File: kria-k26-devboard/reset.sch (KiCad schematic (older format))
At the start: 0 parts

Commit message: Finished reset logic, added crystal gen. to USB PHY, create power toggle for SD 3.0
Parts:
- added C? (x2): C_47n_0402, antmicro-footprints:0402-cap, symbol antmicroCapacitors0402:C_47n_0402
- added C? (x7): C_100n_0402, antmicro-footprints:0402-cap, symbol antmicroCapacitors0402:C_100n_0402
- added R? (x5): R_10k_0402, antmicro-footprints:0402-res, symbol antmicroResistors0402:R_10k_0402
- added S?: KMR2, antmicro-footprints:SW_SPST_4.2x2.8, symbol antmicroPushbuttonSwitches:KMR2
- added U? (x2): TPS3840PH30DBVR, antmicro-footprints:SOT-23-5, symbol antmicroPMICPowerSequencers:TPS3840PH30DBVR
- added U? (x2): SN74AVC4T245PWR, Package_SO:TSSOP-16_4.4x5mm_P0.65mm, symbol antmicroLogicTranslatorsLevelShifters:SN74AVC4T245PWR
- added U? (x6): 74LV07ATPWJ, antmicro-footprints:TSSOP-14_W4.4mm, symbol antmicroLogicGatesandInverters:74LV07ATPWJ
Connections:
- new net: S?.2, S?.4, U?.4 (MR_N), U?.4 (MR_N)
- new net: U?.1 (RESET), U?.14 (2~OE), U?.15 (1~OE) (x2)
- new net: C?.1, U?.5 (CT) (x2)
- new net: U?.1, U?.4 (1A1)
- new net: U?.3, U?.5 (1A2)
- new net: U?.5, U?.6 (2A1)
- new net: U?.7 (2A2), U?.9
- new net: U?.11, U?.4 (1A1)
- new net CAM0_PWDN: U?.5 (1A2)
- new net CAM0_RST: R?.2, U?.10
- new net CAM1_PWDN: U?.6 (2A1)
- new net ETH_RESET: R?.2, U?.8
- new net GND: C?.2, C?.2, C?.2, C?.2, C?.2, C?.2, C?.2, C?.2, C?.2, S?.1, S?.3, U?.10 (2B2), U?.2 (1DIR), U?.2 (1DIR), U?.3 (2DIR), U?.3 (2DIR), U?.3 (GND), U?.3 (GND), U?.7 (GND), U?.8 (GND), U?.8 (GND), U?.9 (GND), U?.9 (GND)
- new net HDA02: U?.13 (1B1)
- new net HDA04: U?.12 (1B2)
- new net HDA09: U?.11 (2B1)
- new net MIO38: U?.10 (2B2)
- new net MIO43: U?.13 (1B1)
- new net MIO44: U?.11 (2B1), U?.12 (1B2)
- new net PL_1V8: U?.16 (VCCB)
- new net PL_3V3: R?.1, U?.2 (VDD)
- new net PS_1V8: C?.1, C?.1, R?.1, R?.1, U?.16 (VCCB)
- new net PS_3V3: C?.1, C?.1, C?.1, C?.1, R?.1, R?.1, U?.1 (VCCA), U?.1 (VCCA), U?.2 (VDD)
- new net SD_CARD_RESET: R?.2, U?.2
- new net SOM_5V: C?.1, U?.14 (VCC)
- new net USB_HUB_RESET: R?.2, U?.6
- new net USB_PHY_RESET: R?.2, U?.4

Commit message: Progress on Debug sheet
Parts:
- gave numbers to parts that had none: 20

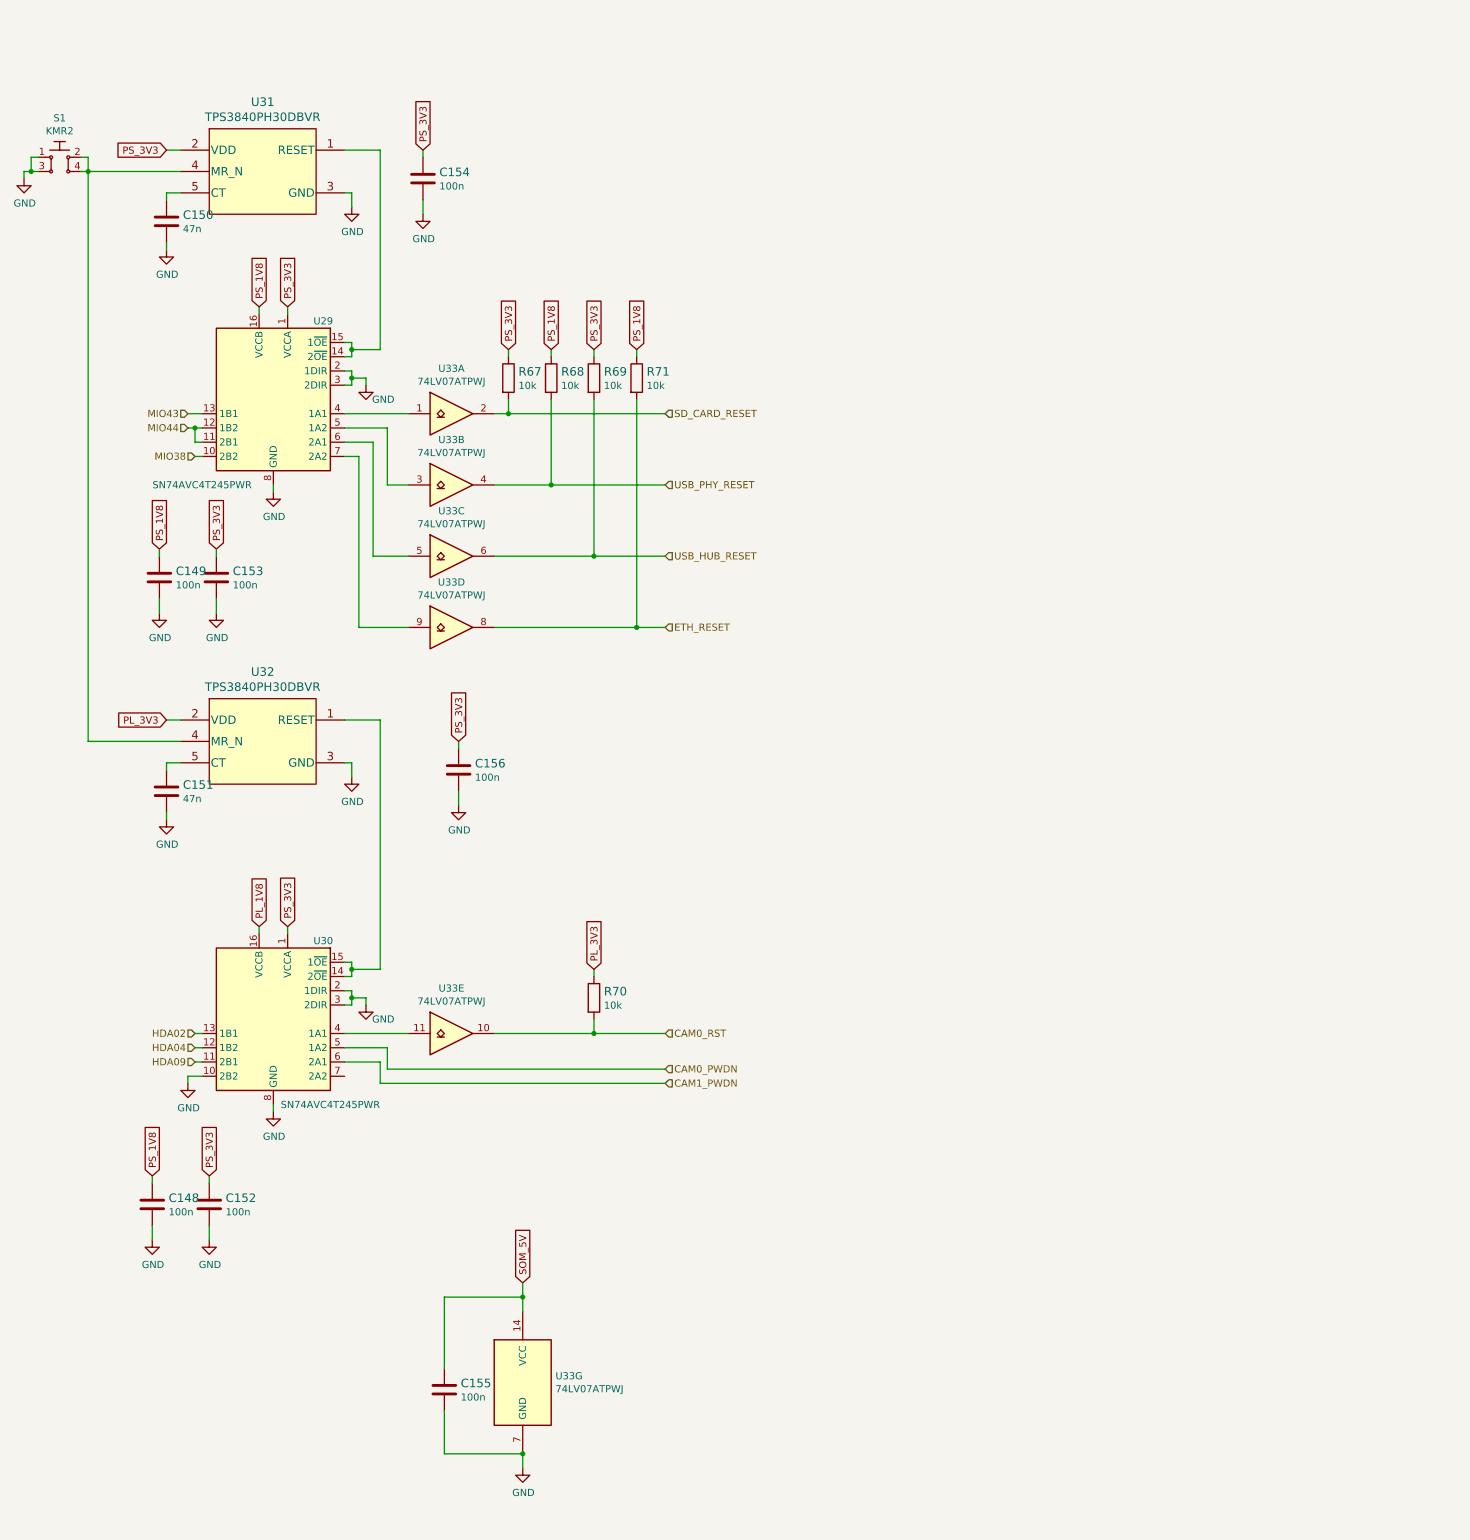
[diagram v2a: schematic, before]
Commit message: Added finished i2c (wirh eeprom) and pmod sheet. Added JTAG connector with collision avoidance logic
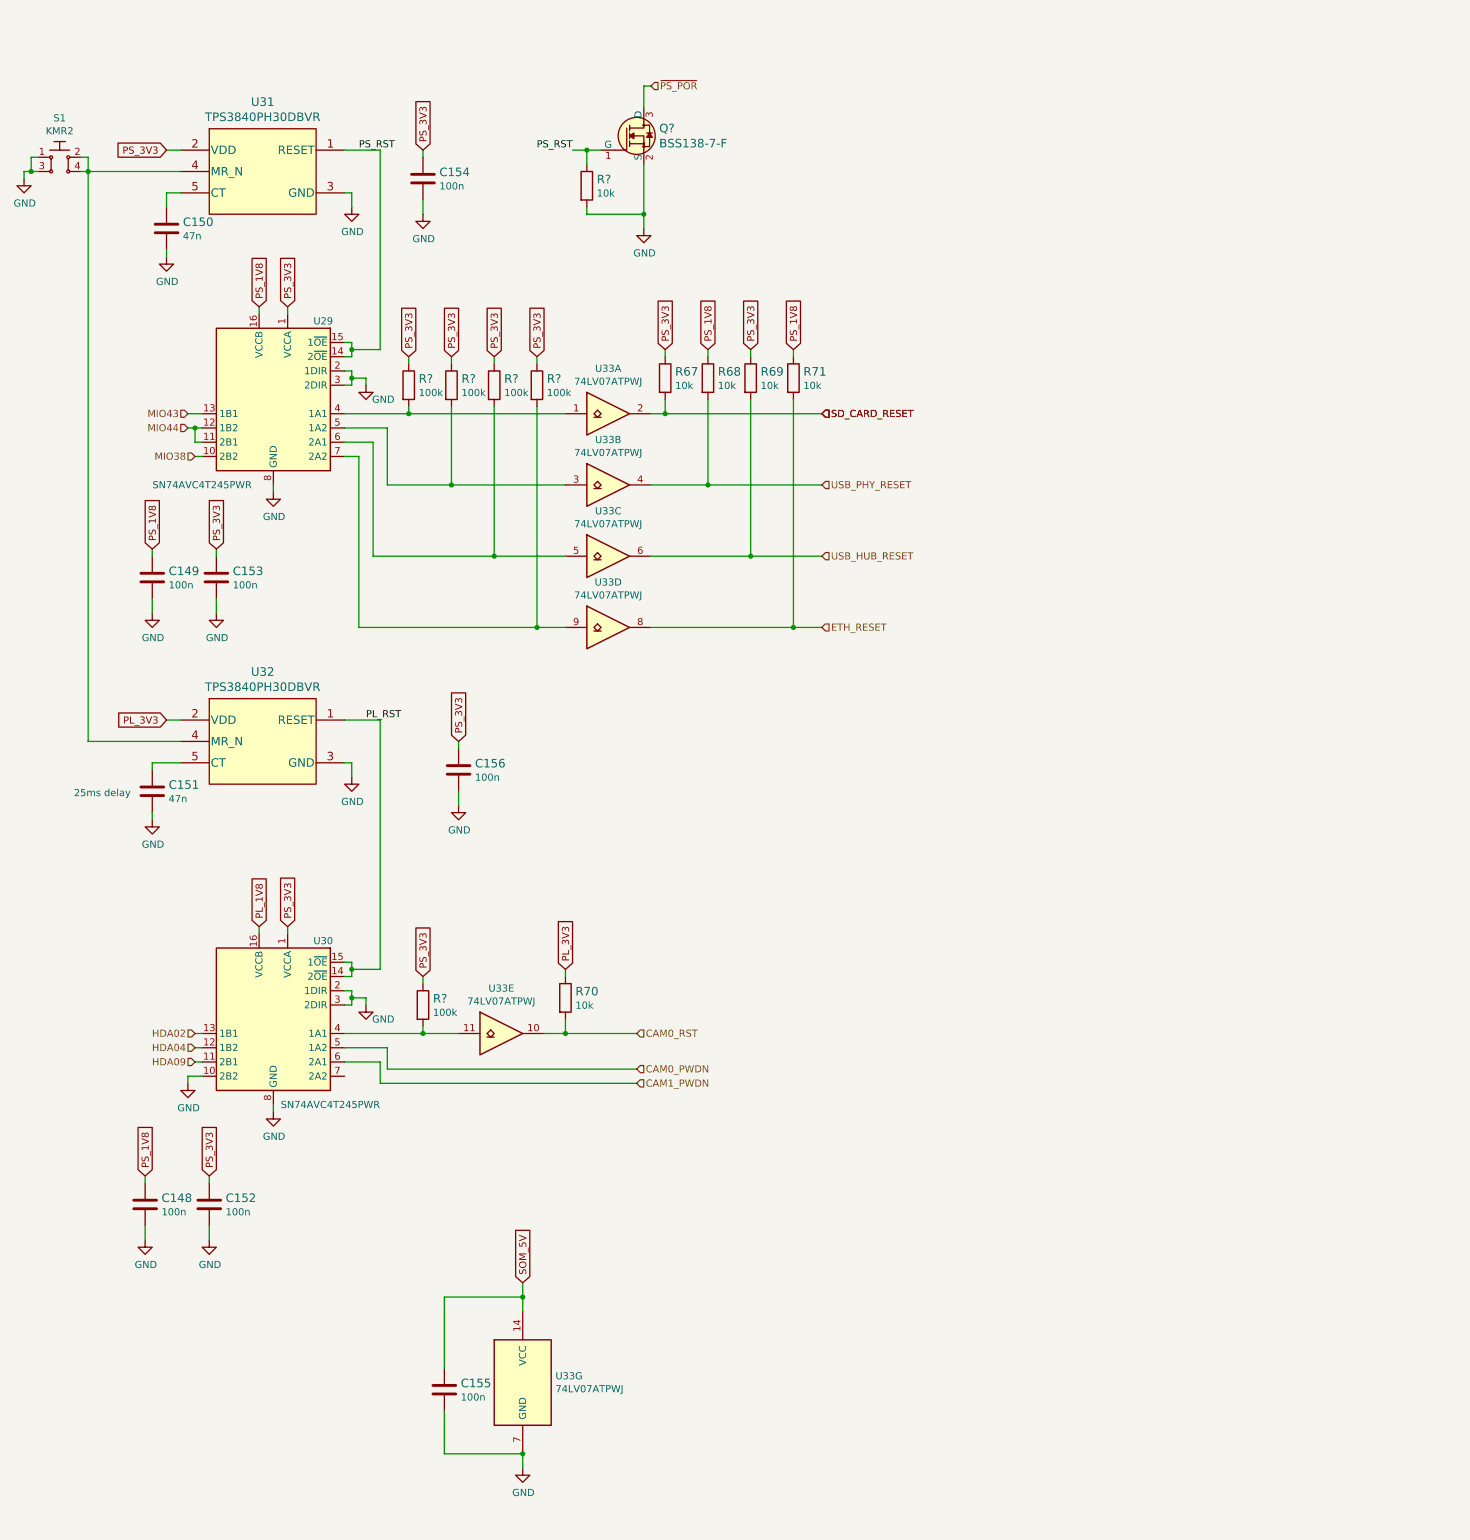
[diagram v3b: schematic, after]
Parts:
- added Q?: BSS138-7-F, antmicro-footprints:SOT-23-3, symbol antmicroTransistorsFETsMOSFETsSingle:BSS138-7-F
- added R?: R_10k_0402, antmicro-footprints:0402-res, symbol antmicroResistors0402:R_10k_0402
- added R? (x5): R_100k_0402, antmicro-footprints:0402-res, symbol antmicroResistors0402:R_100k_0402
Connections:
- net GND: now also Q?.2 (S), R?.2
- net PS_3V3: now also R?.1, R?.1, R?.1, R?.1, R?.1
- net PS_RST: now reaches U29.14 (2~OE), U29.15 (1~OE), U31.1 (RESET)
- net PS_RST: now also Q?.1 (G), R?.1
- net PL_RST: now reaches U30.14 (2~OE), U30.15 (1~OE), U32.1 (RESET)
- net at U29.4 (1A1), U33.1: now also R?.2
- net at U29.5 (1A2), U33.3: now also R?.2
- net at U29.6 (2A1), U33.5: now also R?.2
- net at U29.7 (2A2), U33.9: now also R?.2
- net at U30.4 (1A1), U33.11: now also R?.2
- new net ~PS_POR: Q?.3 (D)
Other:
- note added: "25ms delay"
- moved on the sheet: C148, C149, C150, C151, R67, R68, R69, R70, R71, U33A, U33B, U33C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

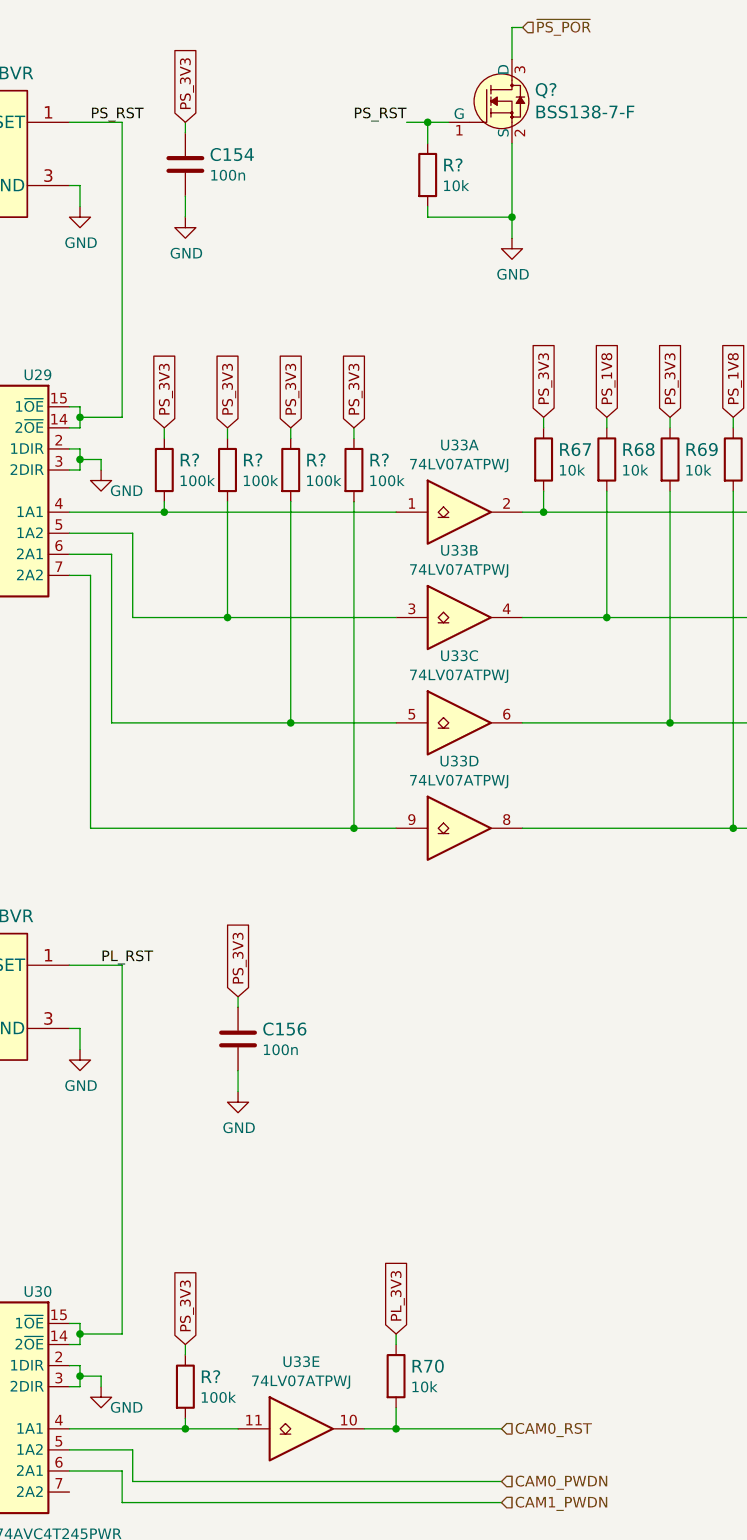
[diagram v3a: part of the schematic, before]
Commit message: Added second ETH interface, connect POE PSE
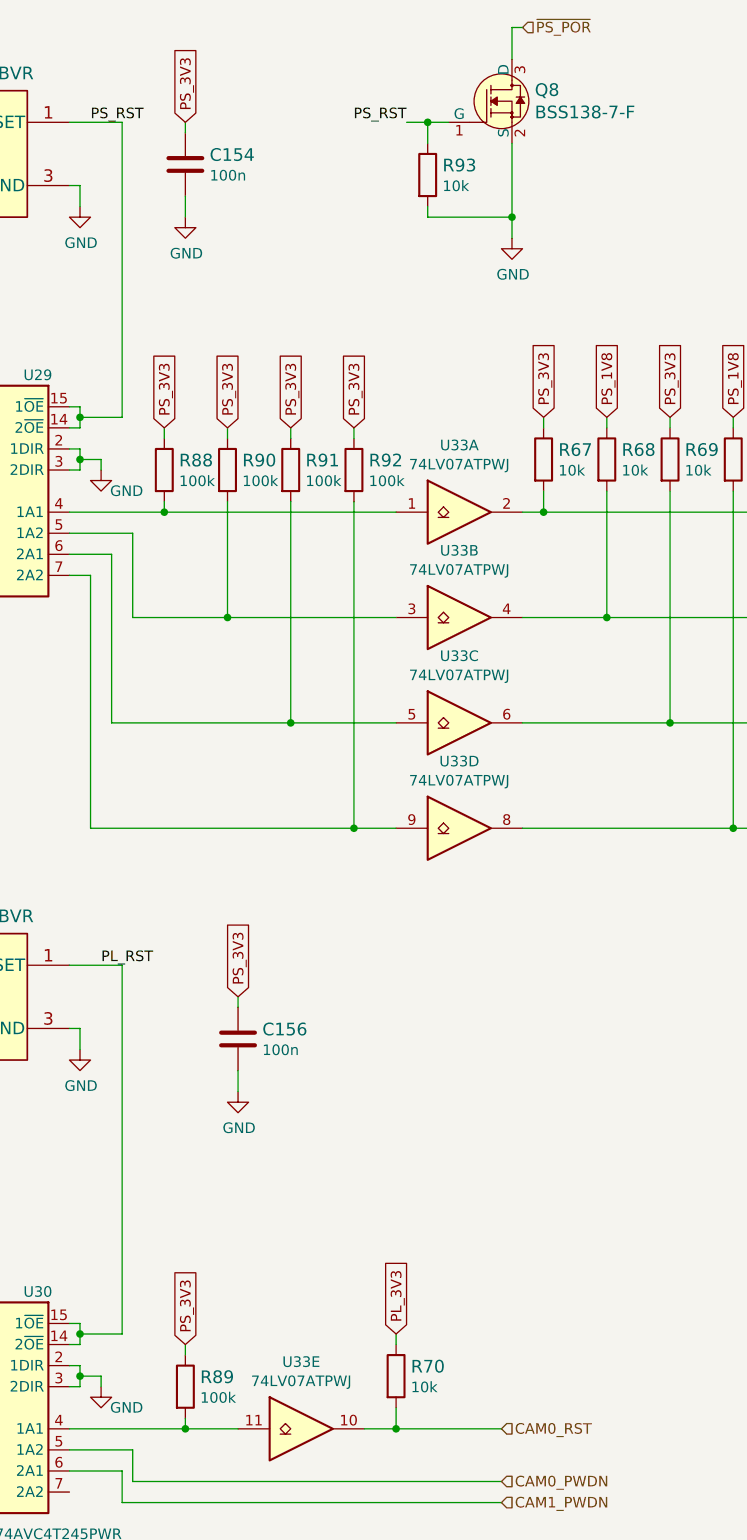
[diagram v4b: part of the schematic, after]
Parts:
- gave numbers to parts that had none: 7
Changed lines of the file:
@@
 HDA09
 $Comp
-L antmicroTransistorsFETsMOSFETsSingle:BSS138-7-F Q?
+L antmicroTransistorsFETsMOSFETsSingle:BSS138-7-F Q8
 U 1 1 63E971C7
 P 10300 1400
-F 0 "Q?" H 10408 1453 60  0000 L CNN
+F 0 "Q8" H 10408 1453 60  0000 L CNN
 F 1 "BSS138-7-F" H 10408 1347 60  0000 L CNN
 F 2 "antmicro-footprints:SOT-23-3" H 10500 1600 60  0001 L CNN
@@
 	9800 1500 9900 1500
 $Comp
-L power:GND #PWR?
+L power:GND #PWR0321
 U 1 1 63EA9D32
 P 10300 2050
-F 0 "#PWR?" H 10300 1800 50  0001 C CNN
+F 0 "#PWR0321" H 10300 1800 50  0001 C CNN
 F 1 "GND" H 10305 1877 50  0000 C CNN
 F 2 "" H 10300 2050 50  0001 C CNN
@@
 	10300 1050 10350 1050
 $Comp
-L antmicroResistors0402:R_10k_0402 R?
+L antmicroResistors0402:R_10k_0402 R93
 U 1 1 63ED8AB3
 P 9900 1750
-F 0 "R?" V 9855 1820 60  0000 L CNN
+F 0 "R93" V 9855 1820 60  0000 L CNN
 F 1 "R_10k_0402" H 9900 1600 60  0001 C CNN
 F 2 "antmicro-footprints:0402-res" H 10100 1950 60  0001 L CNN
@@
 	8750 7700 9000 7700
 $Comp
-L antmicroResistors0402:R_100k_0402 R?
+L antmicroResistors0402:R_100k_0402 R88
 U 1 1 63F973C4
 P 8650 3150
-F 0 "R?" V 8605 3220 60  0000 L CNN
+F 0 "R88" V 8605 3220 60  0000 L CNN
 F 1 "R_100k_0402" H 8650 3000 60  0001 C CNN
 F 2 "antmicro-footprints:0402-res" H 8850 3350 60  0001 L CNN
@@
 $EndComp
 $Comp
-L antmicroResistors0402:R_100k_0402 R?
+L antmicroResistors0402:R_100k_0402 R90
 U 1 1 63F97F51
 P 8950 3150
-F 0 "R?" V 8905 3220 60  0000 L CNN
+F 0 "R90" V 8905 3220 60  0000 L CNN
 F 1 "R_100k_0402" H 8950 3000 60  0001 C CNN
 F 2 "antmicro-footprints:0402-res" H 9150 3350 60  0001 L CNN
@@
 $EndComp
 $Comp
-L antmicroResistors0402:R_100k_0402 R?
+L antmicroResistors0402:R_100k_0402 R91
 U 1 1 63F9876A
 P 9250 3150
-F 0 "R?" V 9205 3220 60  0000 L CNN
+F 0 "R91" V 9205 3220 60  0000 L CNN
 F 1 "R_100k_0402" H 9250 3000 60  0001 C CNN
 F 2 "antmicro-footprints:0402-res" H 9450 3350 60  0001 L CNN
@@
 $EndComp
 $Comp
-L antmicroResistors0402:R_100k_0402 R?
+L antmicroResistors0402:R_100k_0402 R92
 U 1 1 63F98BA5
 P 9550 3150
-F 0 "R?" V 9505 3220 60  0000 L CNN
+F 0 "R92" V 9505 3220 60  0000 L CNN
 F 1 "R_100k_0402" H 9550 3000 60  0001 C CNN
 F 2 "antmicro-footprints:0402-res" H 9750 3350 60  0001 L CNN
@@
 $EndComp
 $Comp
-L antmicroResistors0402:R_100k_0402 R?
+L antmicroResistors0402:R_100k_0402 R89
 U 1 1 63F9A356
 P 8750 7500
-F 0 "R?" V 8705 7570 60  0000 L CNN
+F 0 "R89" V 8705 7570 60  0000 L CNN
 F 1 "R_100k_0402" H 8750 7350 60  0001 C CNN
 F 2 "antmicro-footprints:0402-res" H 8950 7700 60  0001 L CNN
